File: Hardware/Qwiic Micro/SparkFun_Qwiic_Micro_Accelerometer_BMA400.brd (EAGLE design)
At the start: 7.6 x 19.1 mm, 40 parts, among them J1 QWIIC_RIGHT_ANGLE, U1 BMA400

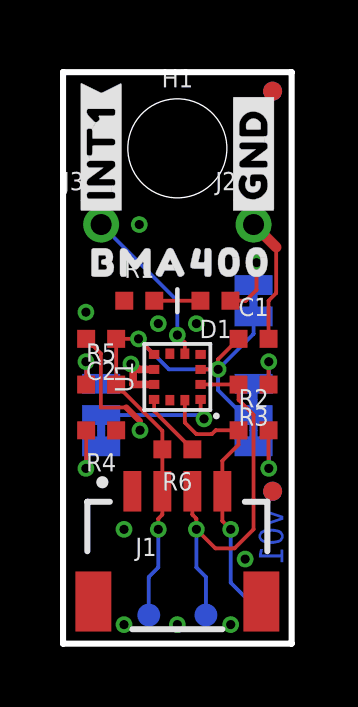
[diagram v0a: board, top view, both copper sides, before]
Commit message: Add axes labels
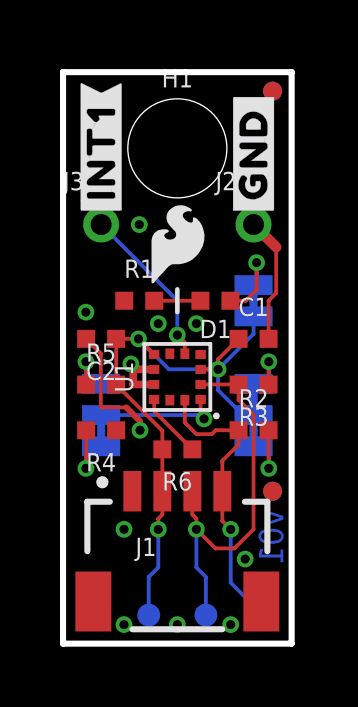
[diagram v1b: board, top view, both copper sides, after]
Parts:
- added U$12: (no value), ISMTopMini:Y2115
- added U$13: (no value), ISMTopMini:Z2116
- added U$6: (no value), ISMTopMini:X2114
- moved LOGO3 10.5 mm to (3.81, 13.2)
- moved U$5 8.39 mm to (4.19, 4.32), flipped to the bottom
- moved LOGO1 0.76 mm to (4.50, 5.28)
- flipped LOGO4 to the top
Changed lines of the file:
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@@
 <text x="7.62" y="-13.97" size="1.778" layer="51" font="vector">Dryw Wade</text>
 <text x="-15.24" y="-2.54" size="1.778" layer="47" font="vector">Units: inches</text>
+<wire x1="3.813175" y1="0.889" x2="3.813175" y2="2.286" width="0.254" layer="22"/>
+<wire x1="3.813175" y1="0.889" x2="3.559175" y2="1.143" width="0.254" layer="22"/>
+<wire x1="3.813175" y1="0.889" x2="4.067175" y2="1.143" width="0.254" layer="22"/>
+<wire x1="6.07695" y1="3.190875" x2="4.80695" y2="3.190875" width="0.254" layer="22"/>
+<wire x1="6.07695" y1="3.190875" x2="5.82295" y2="2.936875" width="0.254" layer="22"/>
+<wire x1="6.07695" y1="3.190875" x2="5.82295" y2="3.444875" width="0.254" layer="22"/>
+<wire x1="5.79755" y1="2.911475" x2="5.79755" y2="3.470275" width="0.254" layer="22"/>
+<wire x1="4.067175" y1="1.143" x2="3.559175" y2="1.143" width="0.254" layer="22"/>
+<circle x="3.75285" y="3.2639" radius="0.5334" width="0.254" layer="22"/>
+<wire x1="4.1148" y1="3.6576" x2="3.3528" y2="2.8956" width="0.254" layer="22"/>
+<wire x1="4.1402" y1="2.8956" x2="3.3782" y2="3.6576" width="0.254" layer="22"/>
 </plain>
 <attributes>
@@
 <attribute name="VALUE" x="2.159" y="1.778" size="0.6096" layer="27" font="vector" ratio="20"/>
 </element>
-<element name="LOGO1" library="SparkFun-Aesthetics" package="QWIIC_3MM" value="QWIIC_LOGO_3MM" x="3.81" y="4.953" smashed="yes" rot="MR0"/>
+<element name="LOGO1" library="SparkFun-Aesthetics" package="QWIIC_3MM" value="QWIIC_LOGO_3MM" x="4.4958" y="5.2832" smashed="yes" rot="MR0"/>
 <element name="LOGO2" library="SparkFun-Aesthetics" package="BLANK" value="SFE_LOGO_NAMEBLANK" x="-19.05" y="-15.24" smashed="yes"/>
-<element name="LOGO3" library="SparkFun-Aesthetics" package="OSHW-LOGO-S" value="OSHW-LOGOS" x="3.81" y="2.667" smashed="yes" rot="MR0"/>
+<element name="LOGO3" library="SparkFun-Aesthetics" package="OSHW-LOGO-S" value="OSHW-LOGOS" x="3.81" y="13.208" smashed="yes" rot="MR0"/>
 <element name="PWR" library="SparkFun-Jumpers" package="SMT-JUMPER_2_NC_TRACE_SILK" package3d_urn="urn:adsk.eagle:package:39281/1" value="JUMPER-SMT_2_NC_TRACE_SILK" x="6.35" y="11.43" smashed="yes" rot="MR270">
 <attribute name="NAME" x="5.207" y="11.43" size="0.6096" layer="26" font="vector" ratio="20" rot="MR270" align="bottom-center"/>
@@
 <element name="U$2" library="output" package="#GND#0" value="" x="6.35" y="14.097" smashed="yes" rot="MR90"/>
 <element name="U$4" library="output" package="#INT1#0" value="" x="1.27" y="14.097" smashed="yes" rot="MR90"/>
-<element name="LOGO4" library="SparkFun-Aesthetics" package="SFE_LOGO_FLAME_.1" value="SFE_LOGO_FLAME.1_INCH" x="3.81" y="13.335" smashed="yes" rot="MR0"/>
-<element name="U$5" library="output" package="BMA4000" value="" x="3.937" y="12.7" smashed="yes"/>
+<element name="LOGO4" library="SparkFun-Aesthetics" package="SFE_LOGO_FLAME_.1" value="SFE_LOGO_FLAME.1_INCH" x="3.81" y="13.335" smashed="yes"/>
+<element name="U$5" library="output" package="BMA4000" value="" x="4.191" y="4.318" smashed="yes" rot="MR0"/>
 <element name="U$7" library="output" package="#I2C#0" value="" x="4.826" y="7.62" smashed="yes" rot="MR90"/>
 <element name="U$8" library="output" package="#ADR#0" value="" x="2.794" y="7.62" smashed="yes" rot="MR90"/>
@@
 <attribute name="VALUE" x="2.413" y="7.62" size="0.6096" layer="28" font="vector" ratio="20" rot="MR270" align="top-center"/>
 </element>
+<element name="U$6" library="ISMTopMini" package="X2114" value="" x="2.921" y="1.905" smashed="yes" rot="MR0"/>
+<element name="U$12" library="ISMTopMini" package="Y2115" value="" x="5.08" y="2.3368" smashed="yes" rot="MR0"/>
+<element name="U$13" library="ISMTopMini" package="Z2116" value="" x="2.4384" y="3.2258" smashed="yes" rot="MR0"/>
 </elements>
 <signals>
@@
 <wire x1="7.104" y1="11.684" x2="6.85" y2="11.43" width="0.127" layer="1"/>
 <wire x1="6.85" y1="11.43" x2="6.85" y2="10.16" width="0.127" layer="1"/>
+<wire x1="2.04" y1="11.43" x2="2.54" y2="13.97" width="0" layer="19" extent="1-1"/>
+<wire x1="0.762" y1="11.049" x2="2.04" y2="11.43" width="0" layer="19" extent="1-1"/>
+<wire x1="0.77" y1="10.16" x2="0.762" y2="11.049" width="0" layer="19" extent="1-1"/>
+<wire x1="1.77" y1="7.112" x2="2.5654" y2="7.112" width="0" layer="19" extent="1-1"/>
+<wire x1="3.175" y1="10.668" x2="2.04" y2="11.43" width="0" layer="19" extent="1-1"/>
+<wire x1="4.445" y1="10.668" x2="3.175" y2="10.668" width="0" layer="19" extent="1-1"/>
+<wire x1="3.035" y1="9.14" x2="3.175" y2="10.668" width="0" layer="19" extent="1-1"/>
+<wire x1="2.31" y1="5.08" x2="2.5654" y2="7.112" width="0" layer="19" extent="1-1"/>
+<wire x1="2.032" y1="3.81" x2="2.31" y2="5.08" width="0" layer="19" extent="1-1"/>
+<wire x1="6.85" y1="10.16" x2="4.445" y2="10.668" width="0" layer="19" extent="1-1"/>
+<wire x1="0.9525" y1="0.9525" x2="2.032" y2="3.81" width="0" layer="19" extent="16-16"/>
+<wire x1="2.032" y1="0.635" x2="0.9525" y2="0.9525" width="0" layer="19" extent="16-16"/>
+<wire x1="3.81" y1="0.635" x2="2.032" y2="0.635" width="0" layer="19" extent="1-1"/>
+<wire x1="5.588" y1="0.635" x2="3.81" y2="0.635" width="0" layer="19" extent="1-1"/>
+<wire x1="6.0706" y1="2.8194" x2="5.588" y2="0.635" width="0" layer="19" extent="1-1"/>
 </signal>
 <signal name="3.3V">

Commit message: Update version number to v10
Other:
- board text added: "v10"
- board text removed: "v01"
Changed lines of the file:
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@@
 <dimension x1="0" y1="19.05" x2="3.81" y2="19.05" x3="1.905" y3="24.13" textsize="1.778" textratio="15" layer="47" unit="inch"/>
 <dimension x1="0" y1="19.05" x2="1.27" y2="19.05" x3="0.635" y3="27.94" textsize="1.778" textratio="15" layer="47" unit="inch"/>
-<text x="6.9342" y="3.556" size="0.8128" layer="16" font="vector" ratio="20" rot="SMR270" align="center">v01</text>
+<text x="6.9342" y="3.556" size="0.8128" layer="16" font="vector" ratio="20" rot="SMR270" align="center">v10</text>
 <rectangle x1="2.9972" y1="8.8646" x2="3.0734" y2="8.9154" layer="41"/>
 <text x="7.62" y="-13.97" size="1.778" layer="51" font="vector">Dryw Wade</text>
@@
 <wire x1="7.104" y1="11.684" x2="6.85" y2="11.43" width="0.127" layer="1"/>
 <wire x1="6.85" y1="11.43" x2="6.85" y2="10.16" width="0.127" layer="1"/>
-<wire x1="2.04" y1="11.43" x2="2.54" y2="13.97" width="0" layer="19" extent="1-1"/>
-<wire x1="0.762" y1="11.049" x2="2.04" y2="11.43" width="0" layer="19" extent="1-1"/>
-<wire x1="0.77" y1="10.16" x2="0.762" y2="11.049" width="0" layer="19" extent="1-1"/>
-<wire x1="1.77" y1="7.112" x2="2.5654" y2="7.112" width="0" layer="19" extent="1-1"/>
-<wire x1="3.175" y1="10.668" x2="2.04" y2="11.43" width="0" layer="19" extent="1-1"/>
-<wire x1="4.445" y1="10.668" x2="3.175" y2="10.668" width="0" layer="19" extent="1-1"/>
-<wire x1="3.035" y1="9.14" x2="3.175" y2="10.668" width="0" layer="19" extent="1-1"/>
-<wire x1="2.31" y1="5.08" x2="2.5654" y2="7.112" width="0" layer="19" extent="1-1"/>
-<wire x1="2.032" y1="3.81" x2="2.31" y2="5.08" width="0" layer="19" extent="1-1"/>
-<wire x1="6.85" y1="10.16" x2="4.445" y2="10.668" width="0" layer="19" extent="1-1"/>
-<wire x1="0.9525" y1="0.9525" x2="2.032" y2="3.81" width="0" layer="19" extent="16-16"/>
-<wire x1="2.032" y1="0.635" x2="0.9525" y2="0.9525" width="0" layer="19" extent="16-16"/>
-<wire x1="3.81" y1="0.635" x2="2.032" y2="0.635" width="0" layer="19" extent="1-1"/>
-<wire x1="5.588" y1="0.635" x2="3.81" y2="0.635" width="0" layer="19" extent="1-1"/>
-<wire x1="6.0706" y1="2.8194" x2="5.588" y2="0.635" width="0" layer="19" extent="1-1"/>
 </signal>
 <signal name="3.3V">

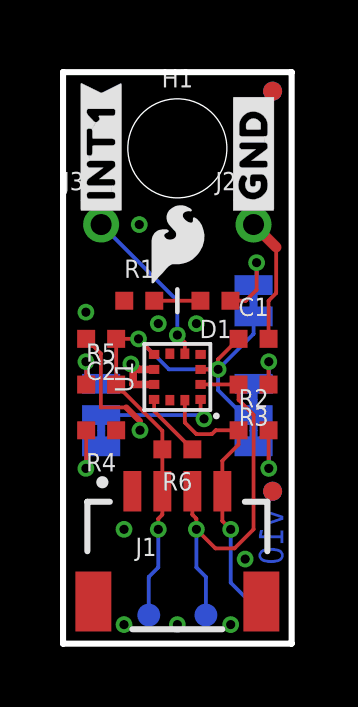
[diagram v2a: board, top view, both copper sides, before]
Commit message: Design review updates
Move fiducials on Micro to be diagonal
Add extra GND vias to Micro
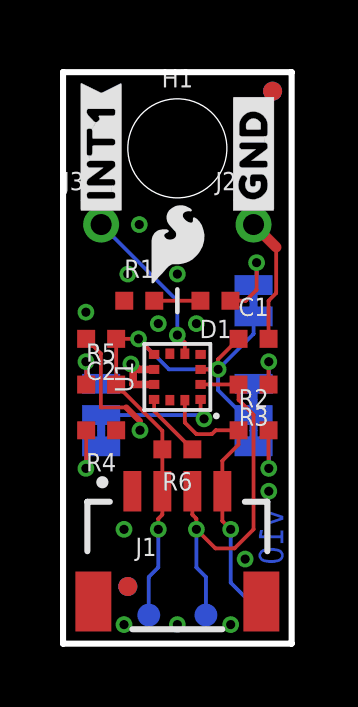
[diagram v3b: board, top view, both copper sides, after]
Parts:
- moved FD1 5.78 mm to (2.16, 1.91)
- moved FD2 5.78 mm to (2.16, 1.91)
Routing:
- net GND: vias 11 -> 14
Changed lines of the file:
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@@
 <attribute name="VALUE" x="5.08" y="12.065" size="0.6096" layer="27" font="vector" ratio="20" rot="R180" align="top-center"/>
 </element>
-<element name="FD1" library="SparkFun-Aesthetics" package="FIDUCIAL-MICRO" value="FIDUCIALUFIDUCIAL" x="6.985" y="5.08" smashed="yes" rot="MR0"/>
-<element name="FD2" library="SparkFun-Aesthetics" package="FIDUCIAL-MICRO" value="FIDUCIALUFIDUCIAL" x="6.985" y="5.08" smashed="yes"/>
+<element name="FD1" library="SparkFun-Aesthetics" package="FIDUCIAL-MICRO" value="FIDUCIALUFIDUCIAL" x="2.159" y="1.905" smashed="yes" rot="MR0"/>
+<element name="FD2" library="SparkFun-Aesthetics" package="FIDUCIAL-MICRO" value="FIDUCIALUFIDUCIAL" x="2.159" y="1.905" smashed="yes"/>
 <element name="FD3" library="SparkFun-Aesthetics" package="FIDUCIAL-MICRO" value="FIDUCIALUFIDUCIAL" x="6.985" y="18.415" smashed="yes"/>
 <element name="FD4" library="SparkFun-Aesthetics" package="FIDUCIAL-MICRO" value="FIDUCIALUFIDUCIAL" x="6.985" y="18.415" smashed="yes" rot="MR0"/>
@@
 <wire x1="7.104" y1="11.684" x2="6.85" y2="11.43" width="0.127" layer="1"/>
 <wire x1="6.85" y1="11.43" x2="6.85" y2="10.16" width="0.127" layer="1"/>
+<via x="6.858" y="5.08" extent="1-16" drill="0.3048"/>
+<via x="3.81" y="12.319" extent="1-16" drill="0.3048"/>
+<via x="2.159" y="12.319" extent="1-16" drill="0.3048"/>
 </signal>
 <signal name="3.3V">

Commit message: Remove library file
Part is in SFE Eagle library, update part in design
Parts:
- U1: device BMA400:BMA400 -> SparkFun-Sensors:BMA400
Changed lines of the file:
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@@
 <attribute name="VALUE" x="3.81" y="7.239" size="0.6096" layer="27" font="vector" ratio="20" rot="R180" align="top-center"/>
 </element>
-<element name="U1" library="BMA400" package="BMA400" value="BMA400" x="3.81" y="8.89" smashed="yes" rot="R90">
+<element name="U1" library="SparkFun-Sensors" package="BMA400" value="BMA400" x="3.81" y="8.89" smashed="yes" rot="R90">
 <attribute name="NAME" x="2.032" y="8.89" size="0.6096" layer="25" font="vector" ratio="20" rot="R90" align="center"/>
 <attribute name="PROD_ID" value="IC-17118" x="3.81" y="8.89" size="1.778" layer="27" rot="R90" display="off"/>
